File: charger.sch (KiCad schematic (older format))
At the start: 22 parts, among them IC1 BQ51050B

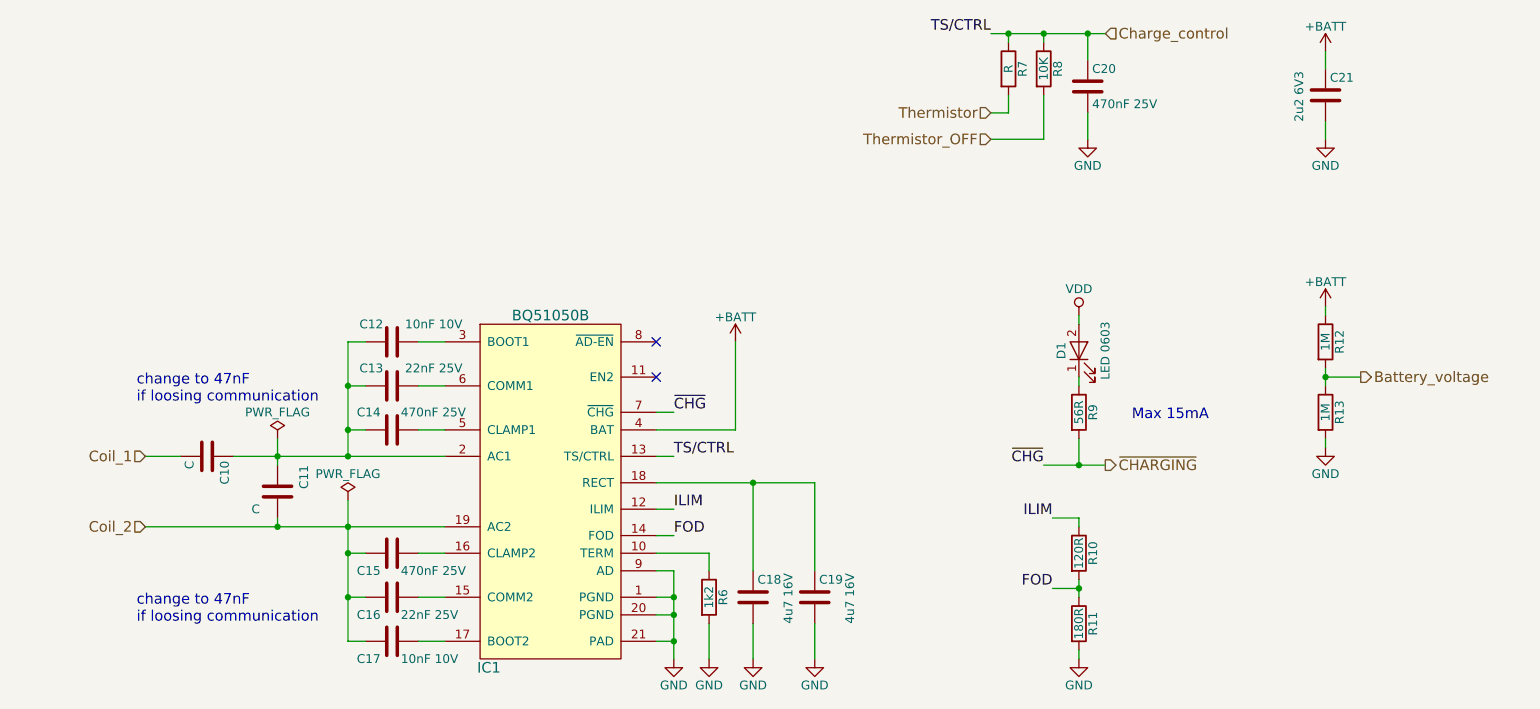
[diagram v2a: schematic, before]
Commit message: Added output stage sheet
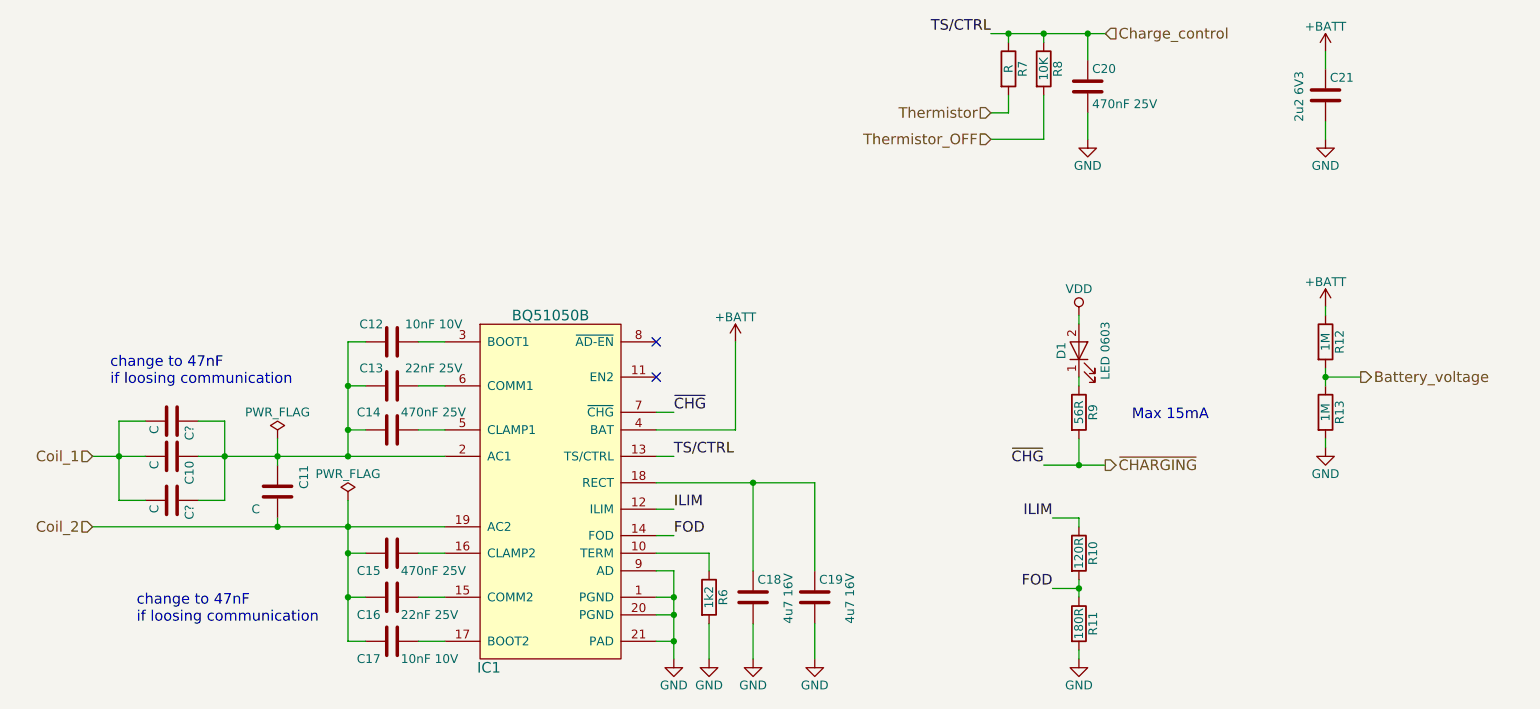
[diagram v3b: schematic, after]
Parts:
- added C? (x2): C, symbol C
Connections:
- net Coil_1: now also C?.2, C?.2
- net at C10.1, C11.2, C12.1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: now also C?.1, C?.1
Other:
- moved on the sheet: C10
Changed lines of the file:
@@
 $Descr A4 11693 8268
 encoding utf-8
-Sheet 3 3
+Sheet 3 4
 Title ""
 Date ""
@@
 Comment4 ""
 $EndDescr
-Text HLabel 1750 3450 0    60   Input ~ 0
+Text HLabel 1450 3450 0    60   Input ~ 0
 Coil_1
-Text HLabel 1750 3850 0    60   Input ~ 0
+Text HLabel 1450 3850 0    60   Input ~ 0
 Coil_2
 Text HLabel 8650 3000 2    60   Output ~ 0
@@
 	0    1    1    0
 $EndComp
-Text Notes 1700 3150 0    60   ~ 0
+Text Notes 1550 3050 0    60   ~ 0
 change to 47nF \nif loosing communication
 Text Notes 1700 4400 0    60   ~ 0
@@
 $EndComp
 Wire Wire Line
-	8450 2950 8450 3050
+	8450 2950 8450 3000
+Wire Wire Line
+	8450 3000 8450 3050
 Wire Wire Line
 	8650 3000 8450 3000
@@
 	4650 4100 4750 4100
 Wire Wire Line
-	4750 4100 4750 4600
+	4750 4100 4750 4250
+Wire Wire Line
+	4750 4250 4750 4350
+Wire Wire Line
+	4750 4350 4750 4500
+Wire Wire Line
+	4750 4500 4750 4600
 Wire Wire Line
 	4650 4250 4750 4250
@@
 	4650 3200 4750 3200
 Wire Wire Line
-	6850 3500 7200 3500
+	6850 3500 7050 3500
+Wire Wire Line
+	7050 3500 7200 3500
 Connection ~ 7050 3500
 Wire Wire Line
@@
 	3300 4000 3450 4000
 Wire Wire Line
-	3000 4000 2900 4000
+	2900 4000 3000 4000
 Connection ~ 2900 4000
 Wire Wire Line
@@
 L C C10
 U 1 1 5AB0567E
-P 2100 3450
-F 0 "C10" H 2125 3550 50  0000 L CNN
-F 1 "C" H 2125 3350 50  0000 L CNN
-F 2 "" H 2138 3300 50  0001 C CNN
-F 3 "" H 2100 3450 50  0001 C CNN
-	1    2100 3450
+P 1900 3450
+F 0 "C10" H 1925 3550 50  0000 L CNN
+F 1 "C" H 1925 3350 50  0000 L CNN
+F 2 "" H 1938 3300 50  0001 C CNN
+F 3 "" H 1900 3450 50  0001 C CNN
+	1    1900 3450
 	0    1    1    0
 $EndComp
 Wire Wire Line
-	1750 3450 1950 3450
-Wire Wire Line
-	2250 3450 3450 3450
-Wire Wire Line
-	2500 3350 2500 3500
+	1450 3450 1600 3450
+Wire Wire Line
+	1600 3450 1750 3450
+Wire Wire Line
+	2050 3450 2200 3450
+Wire Wire Line
+	2200 3450 2500 3450
+Wire Wire Line
+	2500 3450 2900 3450
+Wire Wire Line
+	2900 3450 3450 3450
+Wire Wire Line
+	2500 3350 2500 3450
+Wire Wire Line
+	2500 3450 2500 3500
 Connection ~ 2900 3450
 Connection ~ 2500 3450
 Wire Wire Line
-	1750 3850 3450 3850
+	1450 3850 2500 3850
+Wire Wire Line
+	2500 3850 2900 3850
+Wire Wire Line
+	2900 3850 3450 3850
 Connection ~ 2900 3850
 Wire Wire Line
@@
 Connection ~ 2500 3850
 Wire Wire Line
-	2900 2800 2900 3450
-Wire Wire Line
-	2900 3700 2900 4500
+	2900 2800 2900 3050
+Wire Wire Line
+	2900 3050 2900 3300
+Wire Wire Line
+	2900 3300 2900 3450
+Wire Wire Line
+	2900 3700 2900 3850
+Wire Wire Line
+	2900 3850 2900 4000
+Wire Wire Line
+	2900 4000 2900 4250
+Wire Wire Line
+	2900 4250 2900 4500
 $Comp
 L R R11
@@
 	5200 4100 5200 3600
 Wire Wire Line
-	4650 3600 5550 3600
+	4650 3600 5200 3600
+Wire Wire Line
+	5200 3600 5550 3600
 $Comp
 L GND #PWR40
@@
 $EndComp
 Wire Wire Line
-	6550 1050 7200 1050
+	6550 1050 6650 1050
+Wire Wire Line
+	6650 1050 6850 1050
+Wire Wire Line
+	6850 1050 7100 1050
+Wire Wire Line
+	7100 1050 7200 1050
 Wire Wire Line
 	6650 1050 6650 1100
@@
 FOD
 Wire Wire Line
-	7050 4150 7050 4250
+	7050 4150 7050 4200
+Wire Wire Line
+	7050 4200 7050 4250
 $Comp
 L R R10
@@
 	1    0    0    -1
 $EndComp
+$Comp
+L C C?
+U 1 1 5AC02CB6
+P 1900 3250
+F 0 "C?" H 1925 3350 50  0000 L CNN
+F 1 "C" H 1925 3150 50  0000 L CNN
+F 2 "" H 1938 3100 50  0001 C CNN
+F 3 "" H 1900 3250 50  0001 C CNN
+	1    1900 3250
+	0    1    1    0
+$EndComp
+$Comp
+L C C?
+U 1 1 5AC02DFA
+P 1900 3700
+F 0 "C?" H 1925 3800 50  0000 L CNN
+F 1 "C" H 1925 3600 50  0000 L CNN
+F 2 "" H 1938 3550 50  0001 C CNN
+F 3 "" H 1900 3700 50  0001 C CNN
+	1    1900 3700
+	0    1    1    0
+$EndComp
+Wire Wire Line
+	1600 3700 1750 3700
+Wire Wire Line
+	1600 3250 1600 3450
+Wire Wire Line
+	1600 3450 1600 3700
+Connection ~ 1600 3450
+Wire Wire Line
+	1600 3250 1750 3250
+Wire Wire Line
+	2200 3700 2050 3700
+Wire Wire Line
+	2200 3250 2200 3450
+Wire Wire Line
+	2200 3450 2200 3700
+Connection ~ 2200 3450
+Wire Wire Line
+	2050 3250 2200 3250
 $EndSCHEMATC
